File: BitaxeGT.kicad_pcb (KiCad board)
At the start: 6 copper layers, 65 x 112 mm, 188 parts, among them J1 XT30, J2 Conn_01x08, J3 Conn_01x04, J4 USB_C_Receptacle_USB2.0, J7 Conn_01x04, J8 TC2030-IDC, SW1 SWITCH-SPST, SW2 SWITCH-SPST, U1 TPS546D24S, U10 BM1370_mode1, U11 MCP1824T-1202E/OT, U12 MCP1824T-0802E, U13 EMC2103-2, U2 SN74AVC4T774, U3 TPSM861253RDXR, U4 TPS546D24S, U5 L78L05_SOT89, U6 ESP32-S3-WROOM-1, U8 25MHz, U9 BM1370_mode1

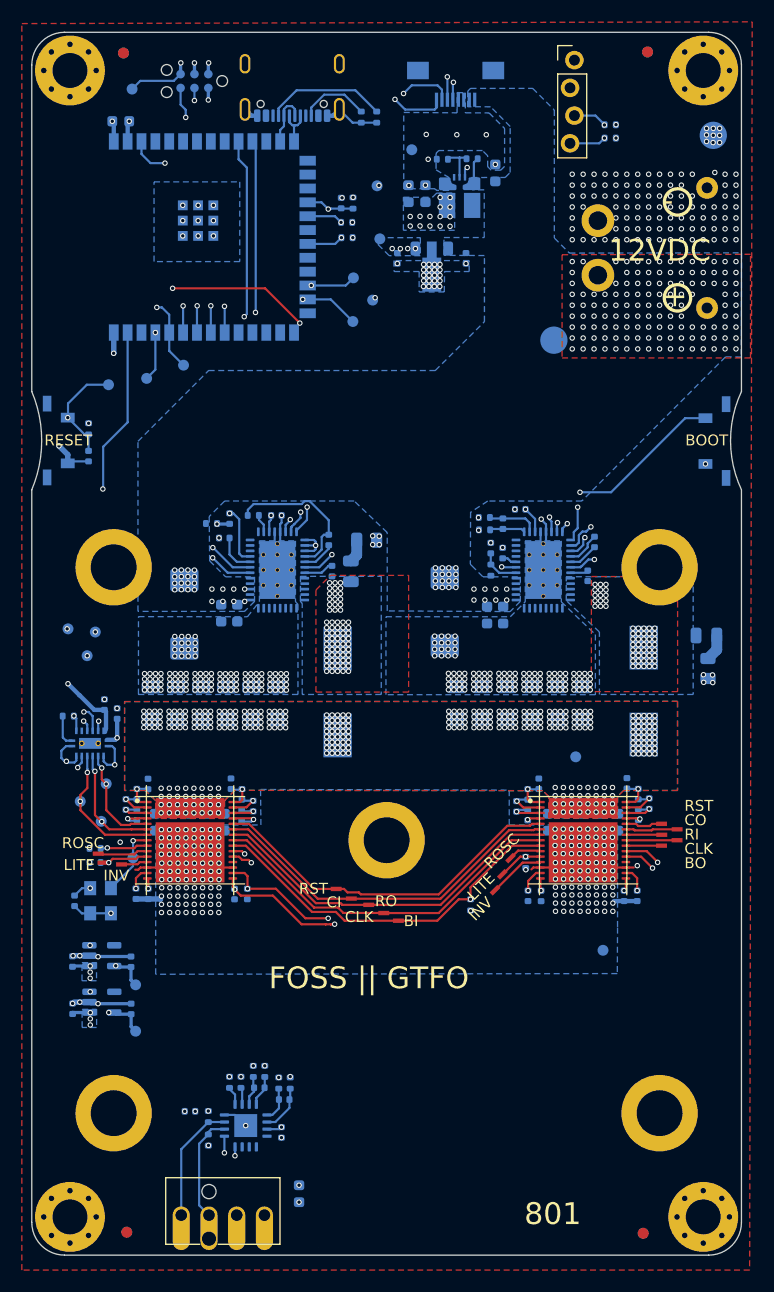
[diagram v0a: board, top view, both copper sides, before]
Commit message: Various changes in PCB
- Updated BM1370 footprint
- Added treaded spacers for heatsink
- Added component references on silkscreen
- Added PM logo
- Added BITAXE logo in solder mask expansion level
- Exported BOM and Gerber files
- Exported PCB 3D file
- Created production specs file
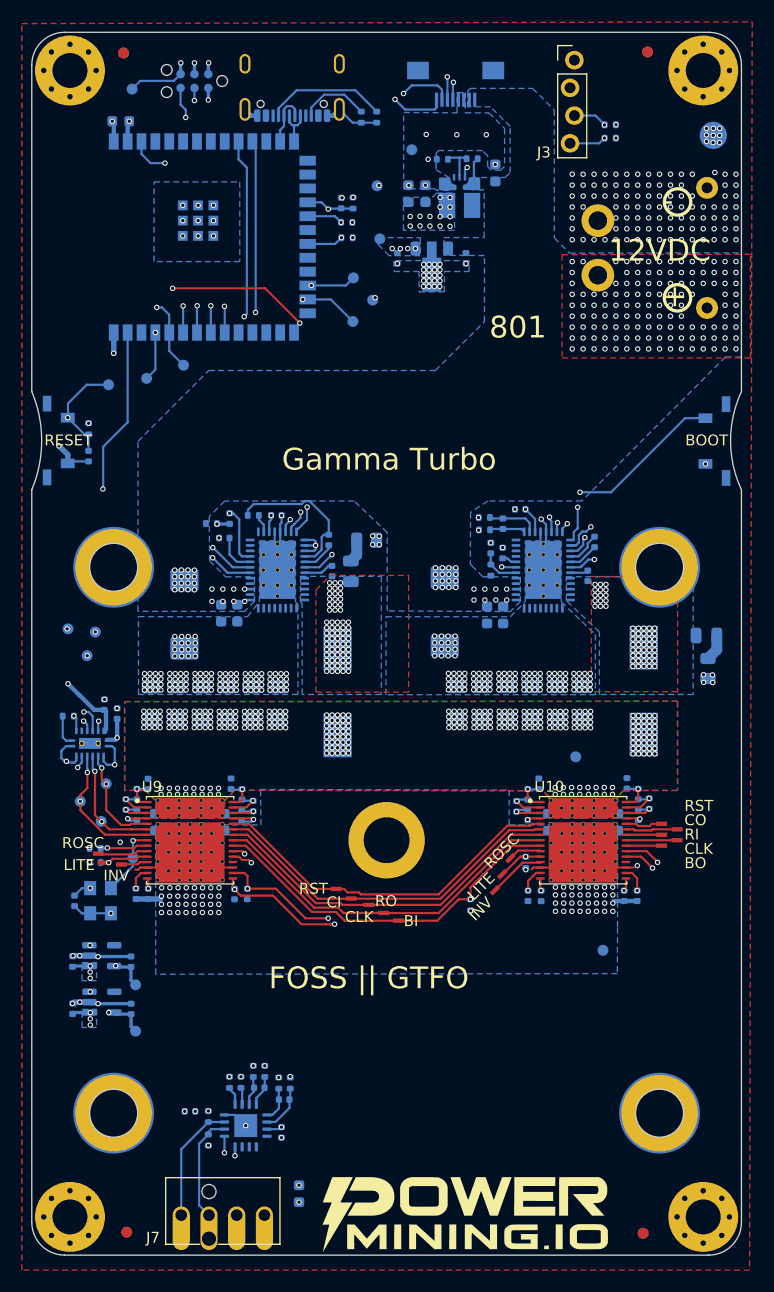
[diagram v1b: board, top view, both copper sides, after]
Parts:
- removed ?: , 
- added J10: Screw_Terminal_01x01, bitaxe:WA-SMSI_9774005360, B.Cu at (156.0, 137.0)
- added J5: Screw_Terminal_01x01, bitaxe:WA-SMSI_9774005360, B.Cu at (106.0, 87.0)
- added J6: Screw_Terminal_01x01, bitaxe:WA-SMSI_9774005360, B.Cu at (156.0, 87.0)
- added J9: Screw_Terminal_01x01, bitaxe:WA-SMSI_9774005360, B.Cu at (106.0, 137.0)
- added Logo: 25mm, bitaxe:PM_logo_25mm, F.Cu at (138.0, 150.5)
- added REF**: CE-Logo_8.5x6mm_SilkScreen, Symbol:CE-Logo_8.5x6mm_SilkScreen, B.Cu at (144.3, 127.4)
- added REF**: UKCA-Logo_6x6mm_SilkScreen, Symbol:UKCA-Logo_6x6mm_SilkScreen, B.Cu at (144.0, 135.6)
- added REF**: FCC-Logo_7.3x6mm_SilkScreen, Symbol:FCC-Logo_7.3x6mm_SilkScreen, B.Cu at (134.0, 127.3)
- added REF**: WEEE-Logo_4.2x6mm_SilkScreen, Symbol:WEEE-Logo_4.2x6mm_SilkScreen, B.Cu at (134.4, 135.5)
- U10, U9: footprint bitaxe:BM1370 -> bitaxe:BM1370_JB
- moved G*** 75.4 mm to (130.6, 70.8)
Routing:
- net GND: vias 590 -> 478
- net /VDD: vias 337 -> 305
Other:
- board text added: "Gamma Turbo"
